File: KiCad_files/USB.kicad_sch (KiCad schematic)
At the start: 4 parts, among them J1 USB_C_Receptacle_USB2.0_16P

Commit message: footprinttejä
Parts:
- removed J1: USB_C_Receptacle_USB2.0_16P, symbol Connector:USB_C_Receptacle_USB2.0_16P
- removed R5: 1M, symbol Device:R
- added J2: USB4105-GF-A, 1_project_library:USB4105_GCT, symbol 1_projektin osat:USB4105-GF-A
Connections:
- net GND: now also J2.A1-B12 (GND)
- net USB_D+: now also J2.A6 (DP1), J2.B6 (DP2)
- net USB_D-: now also J2.A7 (DN1), J2.B7 (DN2)
- net VBUS: now also J2.A4-B9 (VBUS), J2.B4-A9 (VBUS)
- net at R7.1: now also J2.B5 (CC2)
- net at R6.1: now also J2.A5 (CC1)
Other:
- note removed: "TODO Need reverse current protection from battery as we're using both battery and usb power. Also need 5V->3.3V step-down circuit"
- moved on the sheet: R6, R7

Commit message: taikinointia
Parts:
- R6, R7: footprint (none) -> Resistor_SMD:R_0805_2012Metric_Pad1.20x1.40mm_HandSolder
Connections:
- net at J2.B1-A12 (GND): now also J2.B5 (CC2), R7.1
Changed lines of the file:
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@@
+	)
+	(junction
+		(at 203.2 93.98)
+		(diameter 0)
+		(color 0 0 0 0)
 	)
 	(junction
@@
 	(wire
 		(pts
+			(xy 185.42 93.98) (xy 203.2 93.98)
+		)
+		(stroke
+			(width 0)
+			(type default)
+		)
+	)
+	(wire
+		(pts
 			(xy 144.78 86.36) (xy 127 86.36)
 		)
@@
 	(wire
 		(pts
+			(xy 203.2 93.98) (xy 203.2 100.33)
+		)
+		(stroke
+			(width 0)
+			(type default)
+		)
+	)
+	(wire
+		(pts
 			(xy 165.1 64.77) (xy 165.1 68.58)
 		)
@@
 	(wire
 		(pts
-			(xy 203.2 88.9) (xy 203.2 100.33)
+			(xy 203.2 88.9) (xy 203.2 93.98)
 		)
 		(stroke
@@
 			)
 		)
-		(property "Footprint" ""
+		(property "Footprint" "Resistor_SMD:R_0805_2012Metric_Pad1.20x1.40mm_HandSolder"
 			(at 125.222 104.14 90)
 			(effects
@@
 			)
 		)
-		(property "Footprint" ""
+		(property "Footprint" "Resistor_SMD:R_0805_2012Metric_Pad1.20x1.40mm_HandSolder"
 			(at 201.422 104.14 90)
 			(effects

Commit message: update
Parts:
- J2: DigiKey (none) -> 2073-USB4105-GF-ACT-ND
- R6, R7: DigiKey (none) -> P5.1KDACT-ND
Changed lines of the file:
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@@
+			)
+		)
+		(property "DigiKey" "2073-USB4105-GF-ACT-ND"
+			(at 144.78 81.28 0)
+			(effects
+				(font
+					(size 1.27 1.27)
+				)
+				(hide yes)
 			)
 		)
@@
 			)
 		)
+		(property "DigiKey" "P5.1KDACT-ND"
+			(at 127 104.14 0)
+			(effects
+				(font
+					(size 1.27 1.27)
+				)
+				(hide yes)
+			)
+		)
 		(pin "1"
 		)
@@
 			(at 203.2 104.14 0)
 			(effects
+				(font
+					(size 1.27 1.27)
+				)
+				(hide yes)
+			)
+		)
+		(property "DigiKey" "P5.1KDACT-ND"
+			(at 203.2 104.14 0)
+			(effects

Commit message: update
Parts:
- R6, R7: value 5.1K -> 5.1k
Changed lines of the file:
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@@
+			)
+		)
+		(property "Sim.Type" ""
+			(at 144.78 81.28 0)
+			(effects
+				(font
+					(size 1.27 1.27)
+				)
+				(hide yes)
 			)
 		)
@@
 			)
 		)
-		(property "Value" "5.1K"
+		(property "Value" "5.1k"
 			(at 129.54 105.4099 0)
 			(effects
@@
 		)
 		(property "DigiKey" "P5.1KDACT-ND"
+			(at 127 104.14 0)
+			(effects
+				(font
+					(size 1.27 1.27)
+				)
+				(hide yes)
+			)
+		)
+		(property "Sim.Type" ""
 			(at 127 104.14 0)
 			(effects
@@
 			)
 		)
-		(property "Value" "5.1K"
+		(property "Value" "5.1k"
 			(at 205.74 105.4099 0)
 			(effects
@@
 			(at 203.2 104.14 0)
 			(effects
+				(font
+					(size 1.27 1.27)
+				)
+				(hide yes)
+			)
+		)
+		(property "Sim.Type" ""
+			(at 203.2 104.14 0)
+			(effects

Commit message: johtoja
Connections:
- net VBUS renamed USB_VBUS
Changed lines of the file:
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@@
-	(wire
-		(pts
-			(xy 115.57 83.82) (xy 142.24 83.82)
-		)
-		(stroke
-			(width 0)
-			(type default)
-		)
-	)
 	(wire
 		(pts
@@
 	(wire
 		(pts
+			(xy 111.76 83.82) (xy 142.24 83.82)
+		)
+		(stroke
+			(width 0)
+			(type default)
+		)
+	)
+	(wire
+		(pts
 			(xy 127 109.22) (xy 127 107.95)
 		)
@@
 			(width 0)
 			(type default)
+		)
+	)
+	(hierarchical_label "USB_VBUS"
+		(shape output)
+		(at 111.76 83.82 180)
+		(effects
+			(font
+				(size 1.27 1.27)
+			)
+			(justify right)
 		)
 	)
@@
 					(unit 1)
 				)
-			)
-		)
-	)
-	(symbol
-		(lib_id "power:VBUS")
-		(at 115.57 83.82 90)
-		(unit 1)
-		(exclude_from_sim no)
-		(in_bom yes)
-		(on_board yes)
-		(dnp no)
-		(fields_autoplaced yes)
-		(property "Reference" "#PWR017"
-			(at 119.38 83.82 0)
-			(effects
-				(font
-					(size 1.27 1.27)
-				)
-				(hide yes)
-			)
-		)
-		(property "Value" "VBUS"
-			(at 114.3 81.28 90)
-			(effects
-				(font
-					(size 1.27 1.27)
-				)
-			)
-		)
-		(property "Footprint" ""
-			(at 115.57 83.82 0)
-			(effects
-				(font
-					(size 1.27 1.27)
-				)
-				(hide yes)
-			)
-		)
-		(property "Datasheet" ""
-			(at 115.57 83.82 0)
-			(effects
-				(font
-					(size 1.27 1.27)
-				)
-				(hide yes)
-			)
-		)
-		(property "Description" "Power symbol creates a global label with name \"VBUS\""
-			(at 115.57 83.82 0)
-			(effects
-				(font
-					(size 1.27 1.27)
-				)
-				(hide yes)
-			)
-		)
-		(pin "1"
-		)
-		(instances
-			(project "esp"
-				(path "/186d5500-054c-4b47-a89c-85f6ce2abe33/dce605b2-bfca-4721-a3b2-461c5c7ec909"
-					(reference "#PWR017")
-					(unit 1)
-				)

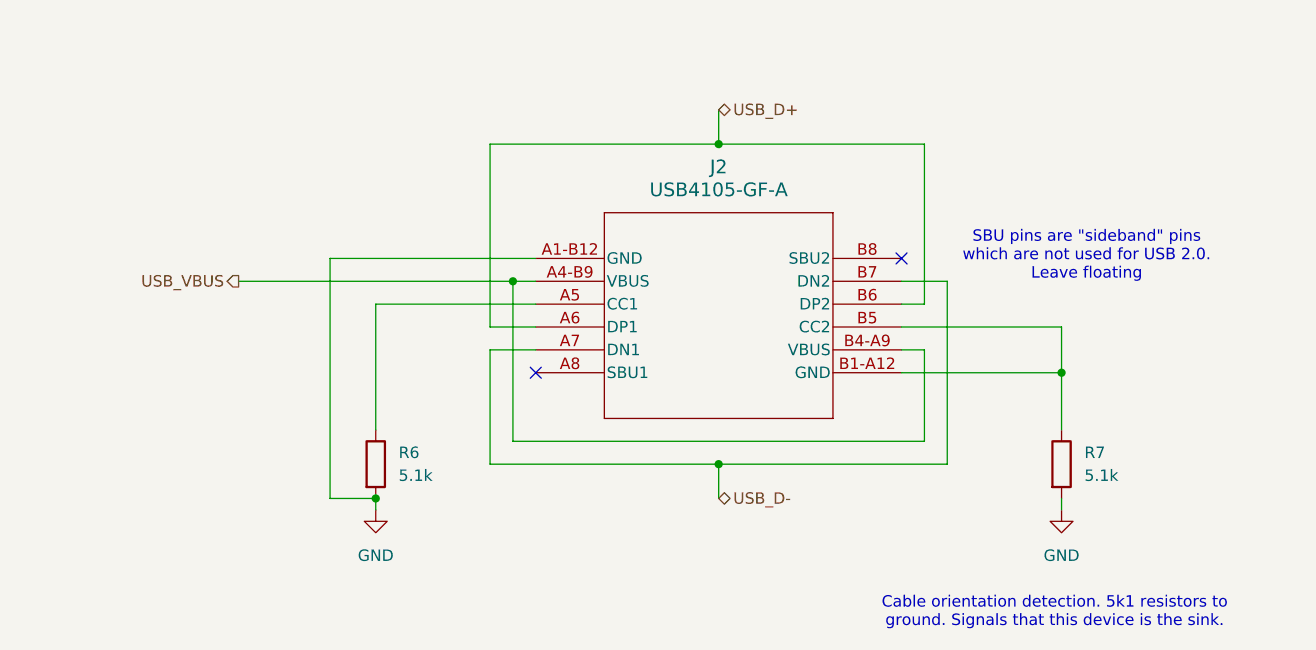
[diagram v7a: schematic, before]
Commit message: piuhat vedetty mculla ja i2c pullupit mculle
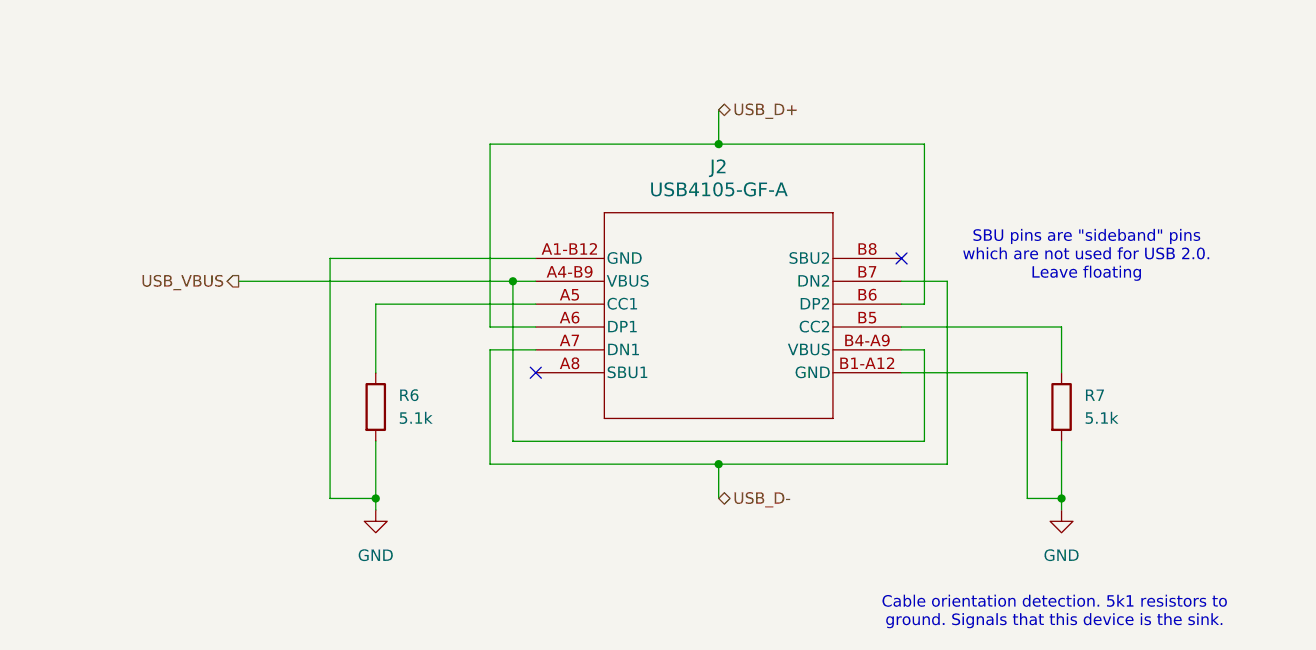
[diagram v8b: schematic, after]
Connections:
- net GND: now also J2.B1-A12 (GND)
- net at J2.B5 (CC2), R7.1: no longer J2.B1-A12 (GND)
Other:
- moved on the sheet: R6, R7
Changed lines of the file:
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@@
-	)
-	(junction
-		(at 203.2 93.98)
-		(diameter 0)
-		(color 0 0 0 0)
 	)
 	(junction
@@
 	)
 	(junction
+		(at 203.2 107.95)
+		(diameter 0)
+		(color 0 0 0 0)
+	)
+	(junction
 		(at 127 107.95)
 		(diameter 0)
@@
 	(wire
 		(pts
+			(xy 185.42 93.98) (xy 199.39 93.98)
+		)
+		(stroke
+			(width 0)
+			(type default)
+		)
+	)
+	(wire
+		(pts
 			(xy 187.96 101.6) (xy 142.24 101.6)
 		)
@@
 	(wire
 		(pts
-			(xy 185.42 93.98) (xy 203.2 93.98)
-		)
-		(stroke
-			(width 0)
-			(type default)
-		)
-	)
-	(wire
-		(pts
 			(xy 144.78 86.36) (xy 127 86.36)
 		)
@@
 	(wire
 		(pts
-			(xy 127 86.36) (xy 127 100.33)
+			(xy 127 86.36) (xy 127 93.98)
 		)
 		(stroke
@@
 	(wire
 		(pts
+			(xy 127 101.6) (xy 127 107.95)
+		)
+		(stroke
+			(width 0)
+			(type default)
+		)
+	)
+	(wire
+		(pts
 			(xy 185.42 83.82) (xy 190.5 83.82)
 		)
@@
 	(wire
 		(pts
+			(xy 199.39 107.95) (xy 203.2 107.95)
+		)
+		(stroke
+			(width 0)
+			(type default)
+		)
+	)
+	(wire
+		(pts
 			(xy 185.42 91.44) (xy 187.96 91.44)
 		)
@@
 	(wire
 		(pts
+			(xy 203.2 101.6) (xy 203.2 107.95)
+		)
+		(stroke
+			(width 0)
+			(type default)
+		)
+	)
+	(wire
+		(pts
 			(xy 190.5 104.14) (xy 165.1 104.14)
 		)
@@
 	(wire
 		(pts
-			(xy 203.2 93.98) (xy 203.2 100.33)
+			(xy 199.39 93.98) (xy 199.39 107.95)
+		)
+		(stroke
+			(width 0)
+			(type default)
+		)
+	)
+	(wire
+		(pts
+			(xy 203.2 88.9) (xy 203.2 93.98)
 		)
 		(stroke
@@
 	(wire
 		(pts
+			(xy 203.2 107.95) (xy 203.2 109.22)
+		)
+		(stroke
+			(width 0)
+			(type default)
+		)
+	)
+	(wire
+		(pts
 			(xy 185.42 86.36) (xy 187.96 86.36)
 		)
@@
 	(wire
 		(pts
-			(xy 203.2 107.95) (xy 203.2 109.22)
-		)
-		(stroke
-			(width 0)
-			(type default)
-		)
-	)
-	(wire
-		(pts
 			(xy 139.7 91.44) (xy 144.78 91.44)
-		)
-		(stroke
-			(width 0)
-			(type default)
-		)
-	)
-	(wire
-		(pts
-			(xy 203.2 88.9) (xy 203.2 93.98)
 		)
 		(stroke
@@
 	(symbol
 		(lib_id "Device:R")
-		(at 127 104.14 0)
+		(at 127 97.79 0)
 		(unit 1)
 		(exclude_from_sim no)
@@
 		(fields_autoplaced yes)
 		(property "Reference" "R6"
-			(at 129.54 102.8699 0)
+			(at 129.54 96.5199 0)
 			(effects
 				(font
@@
 		)
 		(property "Value" "5.1k"
-			(at 129.54 105.4099 0)
+			(at 129.54 99.0599 0)
 			(effects
 				(font
@@
 		)
 		(property "Footprint" "Resistor_SMD:R_0805_2012Metric_Pad1.20x1.40mm_HandSolder"
-			(at 125.222 104.14 90)
+			(at 125.222 97.79 90)
 			(effects
 				(font
@@
 		)
 		(property "Datasheet" "~"
-			(at 127 104.14 0)
+			(at 127 97.79 0)
 			(effects
 				(font
@@
 		)
 		(property "Description" "Resistor"
-			(at 127 104.14 0)
+			(at 127 97.79 0)
 			(effects
 				(font
@@
 		)
 		(property "MNF PART NUMBER" ""
-			(at 127 104.14 0)
+			(at 127 97.79 0)
 			(effects
 				(font
@@
 		)
 		(property "DigiKey" "P5.1KDACT-ND"
-			(at 127 104.14 0)
+			(at 127 97.79 0)
 			(effects
 				(font
@@
 		)
 		(property "Sim.Type" ""
-			(at 127 104.14 0)
+			(at 127 97.79 0)
 			(effects
 				(font
@@
 	(symbol
 		(lib_id "Device:R")
-		(at 203.2 104.14 0)
+		(at 203.2 97.79 0)
 		(unit 1)
 		(exclude_from_sim no)
@@
 		(dnp no)
 		(property "Reference" "R7"
-			(at 205.74 102.8699 0)
+			(at 205.74 96.5199 0)
 			(effects
 				(font
@@
 		)
 		(property "Value" "5.1k"
-			(at 205.74 105.4099 0)
+			(at 205.74 99.0599 0)
 			(effects
 				(font
@@
 		)
 		(property "Footprint" "Resistor_SMD:R_0805_2012Metric_Pad1.20x1.40mm_HandSolder"
-			(at 201.422 104.14 90)
+			(at 201.422 97.79 90)
 			(effects
 				(font
@@
 		)
 		(property "Datasheet" "~"
-			(at 203.2 104.14 0)
+			(at 203.2 97.79 0)
 			(effects
 				(font
@@
 		)
 		(property "Description" "Resistor"
-			(at 203.2 104.14 0)
+			(at 203.2 97.79 0)
 			(effects
 				(font
@@
 		)
 		(property "MNF PART NUMBER" ""
-			(at 203.2 104.14 0)
+			(at 203.2 97.79 0)
 			(effects
 				(font
@@
 		)
 		(property "DigiKey" "P5.1KDACT-ND"
-			(at 203.2 104.14 0)
+			(at 203.2 97.79 0)
 			(effects
 				(font
@@
 		)
 		(property "Sim.Type" ""
-			(at 203.2 104.14 0)
-			(effects
-				(font
+			(at 203.2 97.79 0)
+			(effects
+				(font
